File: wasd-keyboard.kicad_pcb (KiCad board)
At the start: 2 copper layers, 347.5 x 125 mm, 327 parts, among them J1 Conn_01x32, Q1 BC817, SW1 Esc, SW10 F8, SW11 F9, SW12 F10, SW13 F11, SW14 F12, SW15 PrScr, SW16 ScrLock, SW17 Pause, SW18 Tilde, SW19 1, SW2 Reserved, SW20 2, SW21 3, SW22 4, SW23 5, SW24 6, SW25 7, SW26 8, SW27 9, SW28 0, SW29 -, SW3 F1, SW30 +, SW31 JIS |, SW32 JIS Backspace, SW320 Backspace, SW33 Ins, SW34 Home, SW35 PgUp, SW36 Tab, SW37 Q, SW38 W, SW39 E, SW4 F2, SW40 R, SW41 T, SW42 Y, SW43 U, SW44 I, SW45 O, SW46 P, SW47 [, SW48 ], SW49 ANSI \, SW5 F3, SW50 Del, SW51 End, SW52 PgDown, SW53 CapsLock, SW54 A, SW55 S, SW56 D, SW57 F, SW58 G, SW59 H, SW6 F4, SW60 J, SW61 K, SW62 L, SW63 :, SW64 ", SW65 ISO #, SW66 ANSI Enter, SW660 ISO Enter, SW67 ISO L_Shift, SW670 ANSI L_Shift, SW68 ISO \, SW69 Z, SW7 F5, SW70 X, SW71 C, SW72 V, SW73 B, SW74 N, SW75 M, SW76 <, SW77 >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

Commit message: Frame mounting holes fixed
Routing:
- net /ROW6: track 697.6 -> 698.1 mm
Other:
- outline, holes or cut-outs redrawn
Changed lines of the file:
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@@
     (effects (font (size 1 1) (thickness 0.2)))
   )
-  (gr_circle (center 263 214) (end 264.3 214) (layer Edge.Cuts) (width 0.15))
-  (gr_circle (center 74 216) (end 75.3 216) (layer Edge.Cuts) (width 0.15))
+  (gr_circle (center 263 214.2) (end 264.3 214.2) (layer Edge.Cuts) (width 0.15))
+  (gr_circle (center 74.2 216) (end 75.5 216) (layer Edge.Cuts) (width 0.15))
   (gr_circle (center 164.5 205.5) (end 165.8 205.5) (layer Edge.Cuts) (width 0.15))
-  (gr_circle (center 377.5 204.5) (end 378.8 204.5) (layer Edge.Cuts) (width 0.15))
-  (gr_circle (center 337.5 195) (end 338.8 195) (layer Edge.Cuts) (width 0.15))
-  (gr_circle (center 286.5 186) (end 287.8 186) (layer Edge.Cuts) (width 0.15))
+  (gr_circle (center 378.5 204.5) (end 379.8 204.5) (layer Edge.Cuts) (width 0.15))
+  (gr_circle (center 337.9 195.4) (end 339.2 195.4) (layer Edge.Cuts) (width 0.15))
+  (gr_circle (center 286.7 187.5) (end 288 187.5) (layer Edge.Cuts) (width 0.15))
   (gr_circle (center 213.5 166.5) (end 214.8 166.5) (layer Edge.Cuts) (width 0.15))
   (gr_circle (center 117 166.5) (end 118.3 166.5) (layer Edge.Cuts) (width 0.15))
-  (gr_circle (center 377.5 147.5) (end 378.8 147.5) (layer Edge.Cuts) (width 0.15))
-  (gr_circle (center 297.5 124) (end 298.8 124) (layer Edge.Cuts) (width 0.15))
-  (gr_circle (center 359 124) (end 360.3 124) (layer Edge.Cuts) (width 0.15))
-  (gr_circle (center 168 124) (end 169.3 124) (layer Edge.Cuts) (width 0.15))
-  (gr_circle (center 88 124) (end 89.3 124) (layer Edge.Cuts) (width 0.15))
+  (gr_circle (center 378.5 147.5) (end 379.8 147.5) (layer Edge.Cuts) (width 0.15))
+  (gr_circle (center 297.7 124.5) (end 299 124.5) (layer Edge.Cuts) (width 0.15))
+  (gr_circle (center 359.5 124.5) (end 360.8 124.5) (layer Edge.Cuts) (width 0.15))
+  (gr_circle (center 168.1 124.5) (end 169.4 124.5) (layer Edge.Cuts) (width 0.15))
+  (gr_circle (center 88 124.5) (end 89.3 124.5) (layer Edge.Cuts) (width 0.15))
   (gr_circle (center 307.5 166.5) (end 310.1 166.5) (layer Edge.Cuts) (width 0.15))
   (gr_circle (center 140.5 166.5) (end 143.1 166.5) (layer Edge.Cuts) (width 0.15))
@@
   (segment (start 314.3 181.3) (end 310.8 177.8) (width 0.25) (layer B.Cu) (net 196))
   (segment (start 309.2 173.3) (end 306.5 173.3) (width 0.25) (layer B.Cu) (net 196))
-  (segment (start 314.3 181.3) (end 308.2 187.4) (width 0.25) (layer B.Cu) (net 196))
-  (segment (start 308.2 187.4) (end 302.1 187.4) (width 0.25) (layer B.Cu) (net 196))
-  (segment (start 302.1 187.4) (end 298.9 184.2) (width 0.25) (layer B.Cu) (net 196))
-  (segment (start 298.9 184.2) (end 293.4 184.2) (width 0.25) (layer B.Cu) (net 196))
-  (segment (start 293.4 184.2) (end 289 188.6) (width 0.25) (layer B.Cu) (net 196))
-  (segment (start 289 188.6) (end 277.3 188.6) (width 0.25) (layer B.Cu) (net 196))
-  (segment (start 277.3 188.6) (end 276.5 187.8) (width 0.25) (layer B.Cu) (net 196))
-  (segment (start 264.7 187.8) (end 260.5 192) (width 0.25) (layer B.Cu) (net 196))
-  (segment (start 276.5 187.8) (end 264.7 187.8) (width 0.25) (layer B.Cu) (net 196))
-  (segment (start 260.5 192) (end 260.5 192.3) (width 0.25) (layer B.Cu) (net 196))
   (segment (start 306.485 173.3) (end 306.485 170.915) (width 0.25) (layer B.Cu) (net 196))
   (segment (start 306.485 170.915) (end 307.4 170) (width 0.25) (layer B.Cu) (net 196))
@@
   (segment (start 260.2 191.3) (end 260.6 191.7) (width 0.25) (layer B.Cu) (net 196))
   (segment (start 260.6 191.7) (end 260.6 192.1) (width 0.25) (layer B.Cu) (net 196))
+  (segment (start 260.5 192) (end 260.5 192.3) (width 0.25) (layer B.Cu) (net 196))
+  (segment (start 276.5 187.8) (end 264.7 187.8) (width 0.25) (layer B.Cu) (net 196))
+  (segment (start 277.908106 189.208106) (end 276.5 187.8) (width 0.25) (layer B.Cu) (net 196))
+  (segment (start 288.391894 189.208106) (end 277.908106 189.208106) (width 0.25) (layer B.Cu) (net 196))
+  (segment (start 293.4 184.2) (end 288.391894 189.208106) (width 0.25) (layer B.Cu) (net 196))
+  (segment (start 264.7 187.8) (end 260.5 192) (width 0.25) (layer B.Cu) (net 196))
+  (segment (start 314.3 181.3) (end 308.2 187.4) (width 0.25) (layer B.Cu) (net 196))
+  (segment (start 298.9 184.2) (end 293.4 184.2) (width 0.25) (layer B.Cu) (net 196))
+  (segment (start 308.2 187.4) (end 302.1 187.4) (width 0.25) (layer B.Cu) (net 196))
+  (segment (start 302.1 187.4) (end 298.9 184.2) (width 0.25) (layer B.Cu) (net 196))
   (via (at 192.8 109) (size 0.8) (drill 0.4) (layers F.Cu B.Cu) (net 197))
   (segment (start 192.8 109) (end 189.5 109) (width 0.25) (layer B.Cu) (net 197))

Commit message: Fixed switches positions for metal frame
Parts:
- moved SW17 0.90 mm to (385.8, 117.0)
- moved SW35 0.90 mm to (385.8, 143.3)
- moved SW52 0.90 mm to (385.8, 162.3)
- moved SW83 0.90 mm to (385.8, 200.3)
- moved SW97 0.90 mm to (385.8, 219.3)
- moved SW16 0.85 mm to (366.8, 117.0)
- moved SW34 0.85 mm to (366.8, 143.3)
- moved SW51 0.85 mm to (366.8, 162.3)
- moved SW82 0.85 mm to (366.8, 200.3)
- moved SW96 0.85 mm to (366.8, 219.3)
- moved SW15 0.80 mm to (347.7, 117.0)
- moved SW33 0.80 mm to (347.7, 143.3)
- moved SW50 0.80 mm to (347.7, 162.3)
- moved SW81 0.80 mm to (347.7, 200.3)
- moved SW95 0.80 mm to (347.7, 219.3)
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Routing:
- net /ROW14: track 536.7 -> 541.7 mm
- net /ROW12: track 459.3 -> 462.9 mm
- net /ROW3: track 402.8 -> 405.2 mm
- net /ROW10: track 607.8 -> 609.6 mm
- net /80D: track 15.4 -> 17.1 mm
- net /ROW13: track 524.1 -> 525.8 mm
- net /ROW7: track 440.3 -> 441.9 mm
- net /ROW11: track 482.4 -> 484.0 mm
- net /COL5: track 464.6 -> 466.0 mm
- net /ROW9: track 375.5 -> 376.9 mm
- net /ROW2: track 558.0 -> 559.2 mm
- net Net-(D78-Pad2): track 5.54 -> 6.76 mm
- net Net-(D64-Pad2): track 5.43 -> 6.65 mm
- net Net-(R81-Pad1): track 2.41 -> 3.60 mm
- net Net-(R83-Pad1): track 2.51 -> 3.70 mm
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
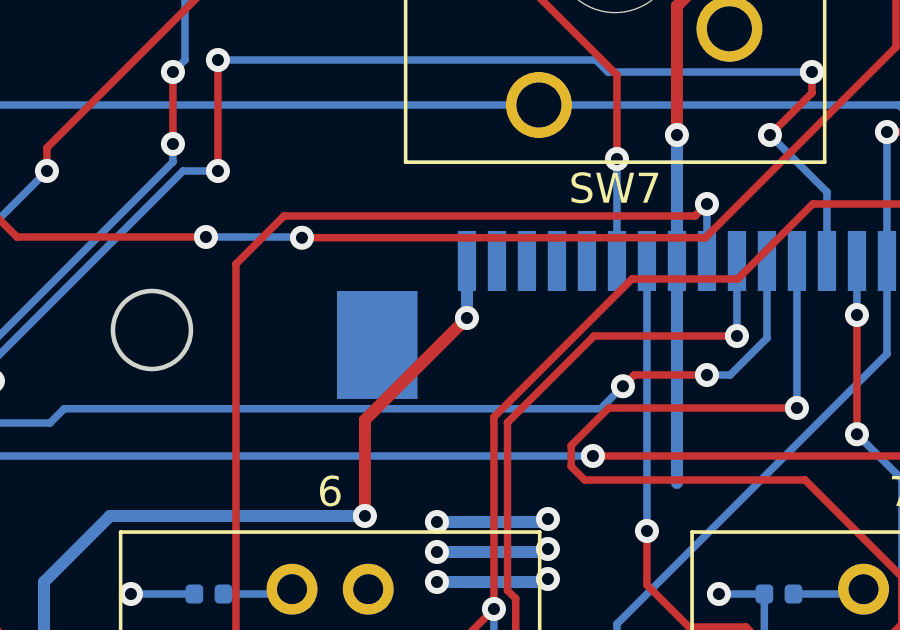
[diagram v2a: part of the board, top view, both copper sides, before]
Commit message: J1 (32 pins) changed to 30 pins for using TE connector
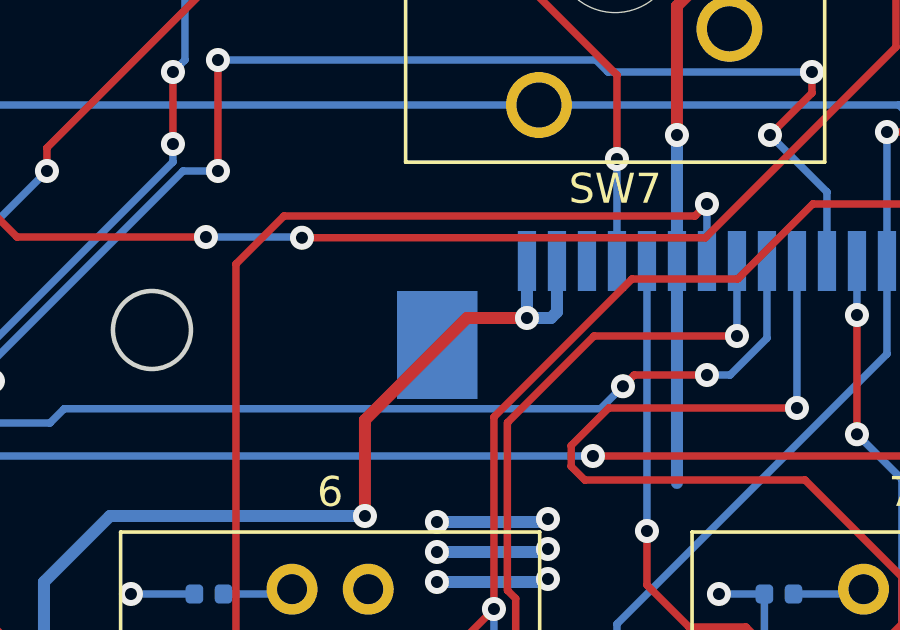
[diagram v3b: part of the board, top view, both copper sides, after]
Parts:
- J1: value Conn_01x32 -> Conn_01x30; footprint wasd-keyboard:Noname_1x32-1MP_P1.0mm_Horizontal -> Connector_FFC-FPC:TE_3-84953-0_1x30-1MP_P1.0mm_Horizontal
- moved J1 1.00 mm to (195.1, 124.0)
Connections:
- J1 pad 28: (no net) -> +5V
- J1 pad 29: (no net) -> GND
- J1 pad 30: (no net) -> GND
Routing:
- net GND: track 859.7 -> 864.5 mm
